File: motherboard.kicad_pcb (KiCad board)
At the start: 2 copper layers, 90.2 x 95.9 mm, 110 parts, among them P1 CONN_02X08, U1 STM32F411-LQFP64, U10 74LS125, U11 74LS125, U12 74LS125, U13 74LS125, U14 PCA9517A, U15 PCA9517A, U16 74LS125, U17 74LS125, U2 STM32F411-LQFP64, U3 AP7313, U4 74LS00, U5 74LS125, U6 FM25V20A-G, U7 FM25V20A-G, U8 FM25V20A-G, U9 FM25V20A-G, Y1 32k, Y2 8M(16pF), Y3 32k, Y4 8M(16pF)

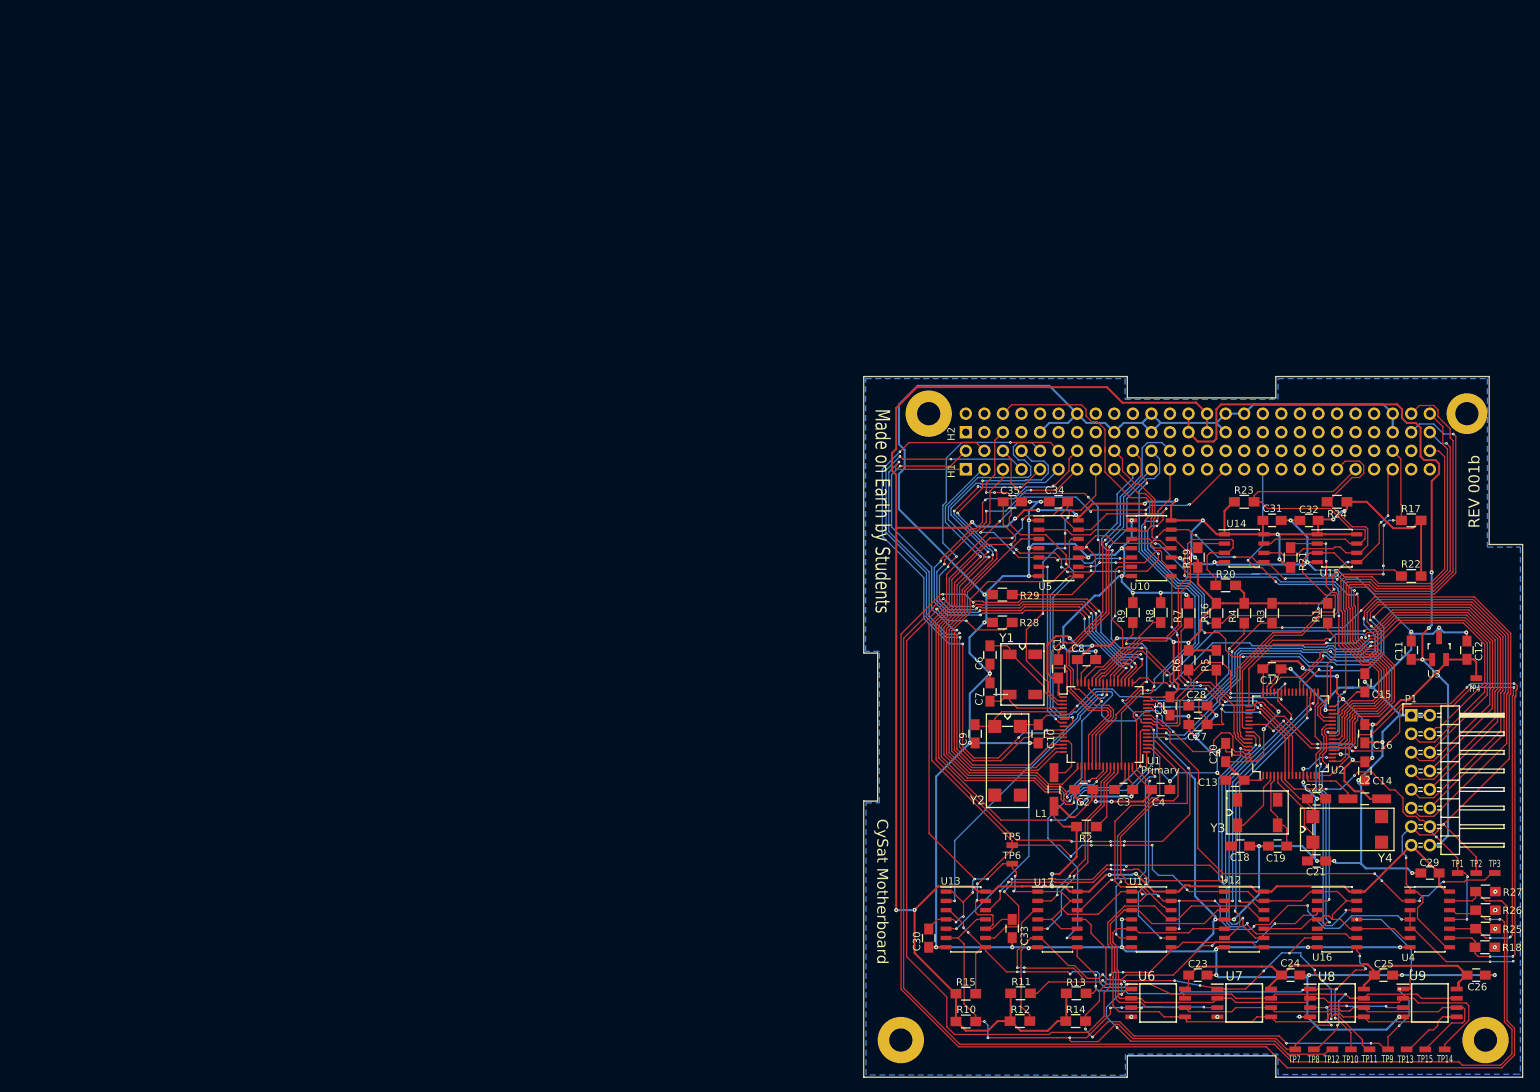
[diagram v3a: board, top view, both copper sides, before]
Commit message: Partial rerouting following resistor movement
Moving the fixed Pull-Up resistors to NAND output made a bunch of
traces have to move.

Not yet complete.
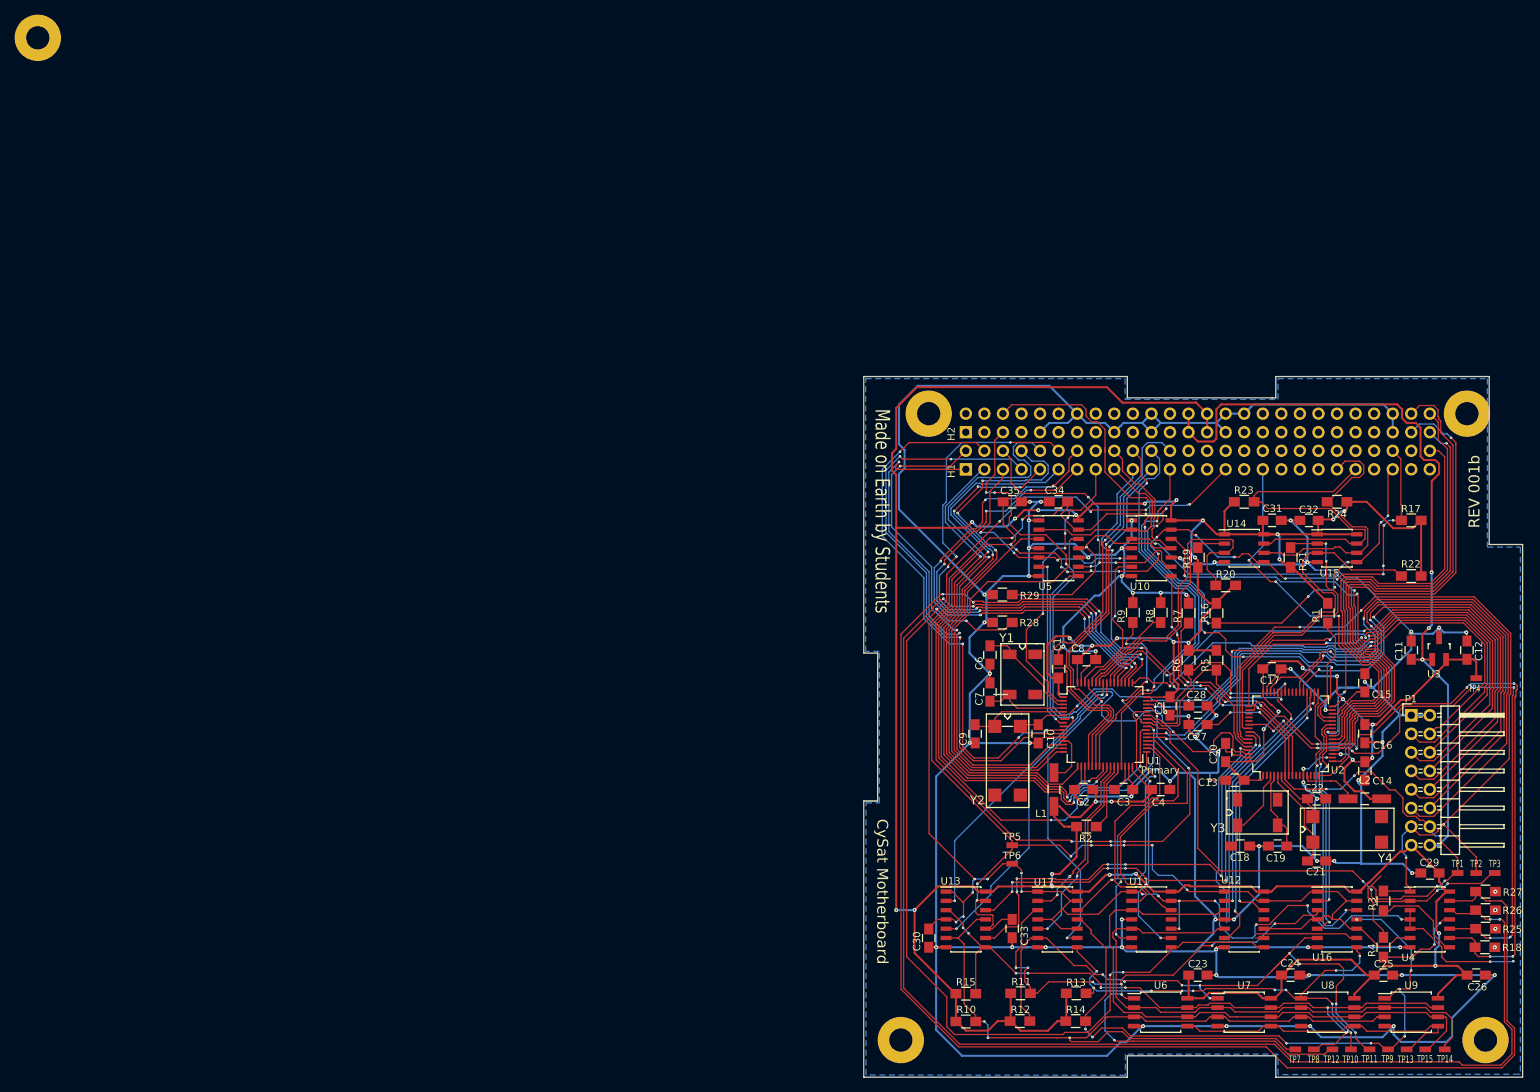
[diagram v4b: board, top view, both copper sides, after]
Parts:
- added REF**: Hole_0.125-0.250, Hole_0.125-0.250, F.Cu at (0.00, 0.00)
- U6, U7, U8, U9: footprint FM25V20A-G:SOIC127P800X203-8N -> Housings_SOIC:SOIJ-8_5.3x5.3mm_Pitch1.27mm
- moved R4 49.5 mm to (184.2, 124.5)
- moved R3 42.2 mm to (184.2, 118.1)
- moved U9 2.84 mm to (188.0, 133.3)
- moved U8 1.80 mm to (176.5, 133.3)
- moved U6 1.32 mm to (153.7, 133.3)
- moved U7 1.27 mm to (165.1, 133.3)
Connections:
- net /NRST1_P renamed /RST1_P
- net /NRST1_S renamed /RST1_S
- net /NRST2_P renamed /RST2_P
- net /NRST2_S renamed /RST2_S
- C33 pad 1: Net-(C33-Pad1) -> /NBUFEN_SEC
- C33 pad 2: Net-(C33-Pad2) -> GND
- C35 pad 1: Net-(C35-Pad1) -> /NBUFEN_SEC
- C35 pad 2: Net-(C35-Pad2) -> GND
- R3 pad 1: /NRST_P -> Net-(R3-Pad1)
- R3 pad 2: +3V3 -> /NRST_P
- R4 pad 1: /NRST_S -> Net-(R4-Pad1)
- R4 pad 2: +3V3 -> /NRST_S
- U4 pad 11: /NRST_S -> Net-(R4-Pad1)
- U4 pad 8: /NRST_P -> Net-(R3-Pad1)
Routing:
- net GND: track 725.5 -> 818.6 mm
- net /MEM_MOSI: track 94.4 -> 42.2 mm
- net Net-(R4-Pad1): track 0.00 -> 12.9 mm, vias 0 -> 2
- net Net-(R3-Pad1): track 0.00 -> 12.7 mm
- net +3V3: track 549.7 -> 558.8 mm, vias 25 -> 27
- net /NRST_P: track 140.2 -> 132.1 mm
- net /NBUFEN_SEC: track 235.4 -> 243.4 mm
- net /MEM_CS2: track 78.2 -> 85.8 mm
- net Net-(C35-Pad1): track 5.90 -> 0.00 mm
- net /SYS_RESET_S: track 42.7 -> 36.9 mm, vias 2 -> 1
- net /MEM_CS1_S: track 46.1 -> 41.1 mm, vias 2 -> 1
- net /MEM_SCK: track 87.1 -> 82.2 mm
- net /NRST_S: track 81.5 -> 77.2 mm, vias 9 -> 7
- net /MEM_MISO: track 82.3 -> 78.2 mm
- net /MEM_NHOLD: track 94.4 -> 92.0 mm
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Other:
- net class Power: clearance 0.2794 -> 0.1778

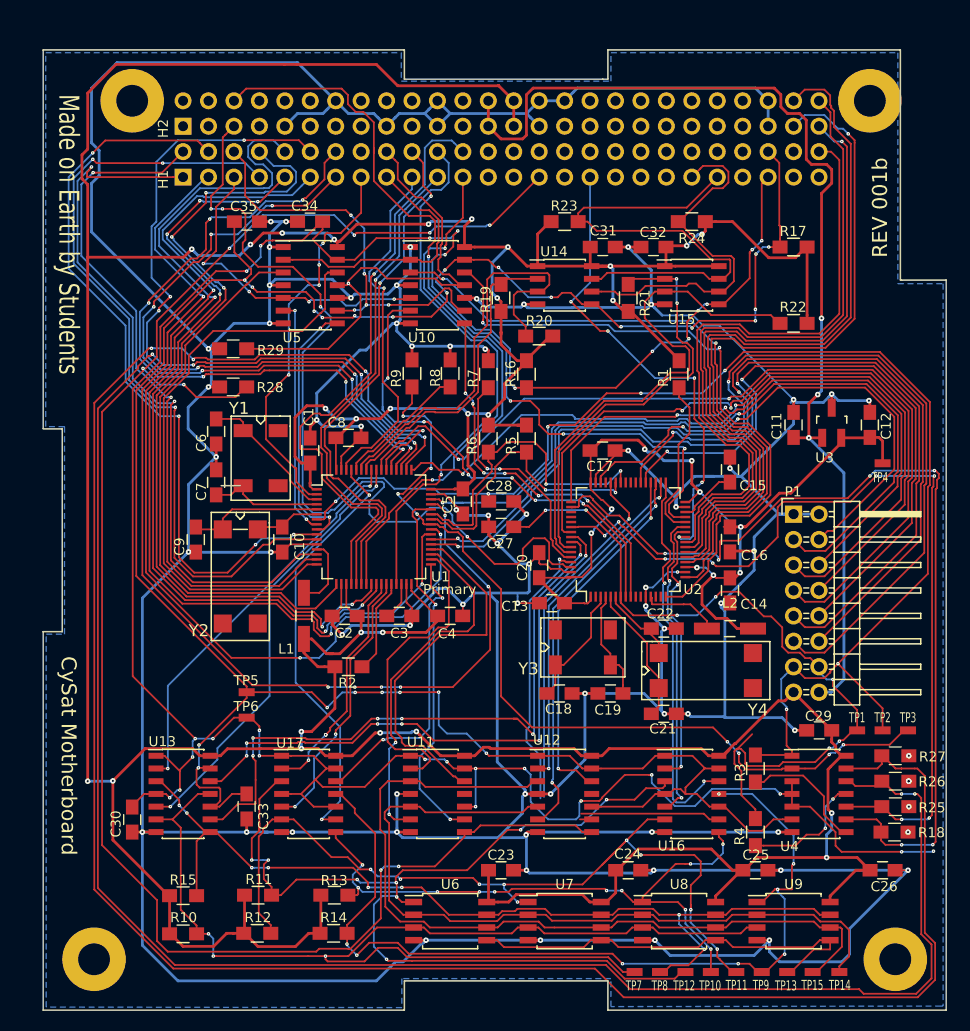
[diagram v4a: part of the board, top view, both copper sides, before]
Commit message: Finished Rev2 reworks
- Addressed documented issues
- Some SGPIO is not connected (see schematic for details)
- Created direct return paths for MEM_SPI
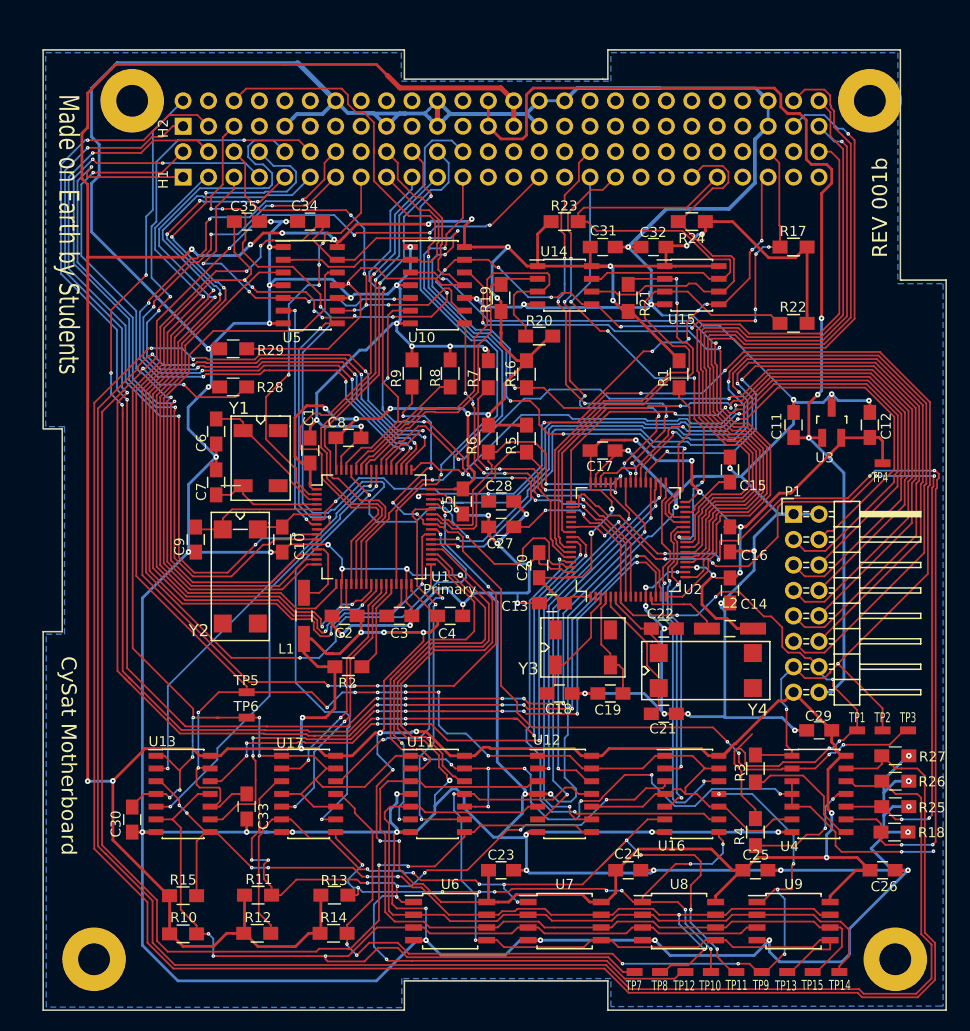
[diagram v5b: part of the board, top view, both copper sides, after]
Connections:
- H1 pad 36: /SGPIO10 -> Net-(H1-Pad36)
- H1 pad 37: /SGPIO11 -> Net-(H1-Pad37)
- H1 pad 38: /SGPIO12 -> Net-(H1-Pad38)
- H1 pad 39: /SGPIO13 -> Net-(H1-Pad39)
- H1 pad 50: /SGPIO5 -> Net-(H1-Pad50)
- H2 pad 4: /SGPIO3 -> Net-(H2-Pad4)
- H2 pad 7: /SGPIO4 -> Net-(H2-Pad7)
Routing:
- net GND: track 818.6 -> 997.0 mm, vias 71 -> 78
- net /SGPIO2: track 0.00 -> 143.8 mm, vias 0 -> 8
- net /SGPIO0: track 0.00 -> 139.7 mm, vias 0 -> 8
- net /SGPIO1: track 0.00 -> 133.0 mm, vias 0 -> 9
- net /SGPIO8: track 0.00 -> 45.7 mm, vias 0 -> 6
- net /SGPIO9: track 0.00 -> 43.6 mm, vias 0 -> 6
- net +3V3: track 558.8 -> 599.6 mm, vias 27 -> 31
- net /MEM_MOSI: track 42.2 -> 73.5 mm, vias 0 -> 2
- net /SYS_RESET_S: track 36.9 -> 41.9 mm, vias 1 -> 2
- net /MEM_CS1_S: track 41.1 -> 45.9 mm, vias 1 -> 2
- net /GPIO8: track 98.8 -> 102.3 mm
- net /NBUFEN_PRI: track 272.6 -> 275.9 mm, vias 29 -> 28
- net /MEM_SCK_P: track 30.9 -> 32.9 mm
- net /MEM_CS1_P: track 42.7 -> 44.7 mm
- net /SYS_RESET_P: track 36.9 -> 38.6 mm
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
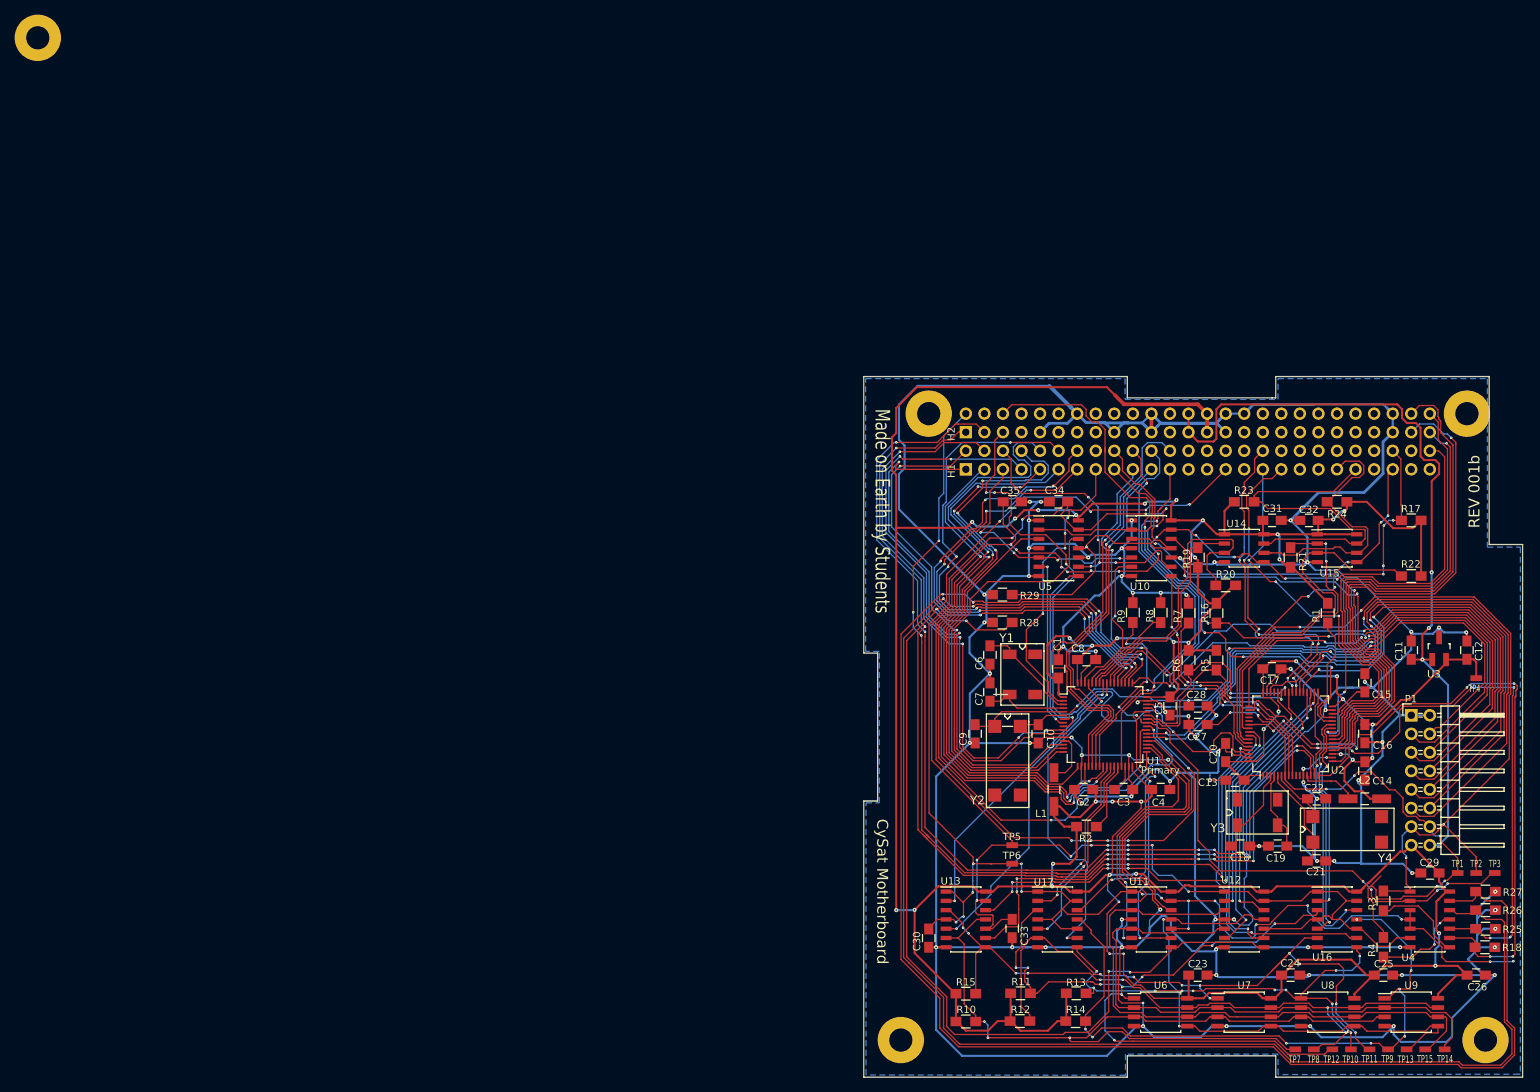
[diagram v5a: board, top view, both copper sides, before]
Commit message: Changed revision number on board
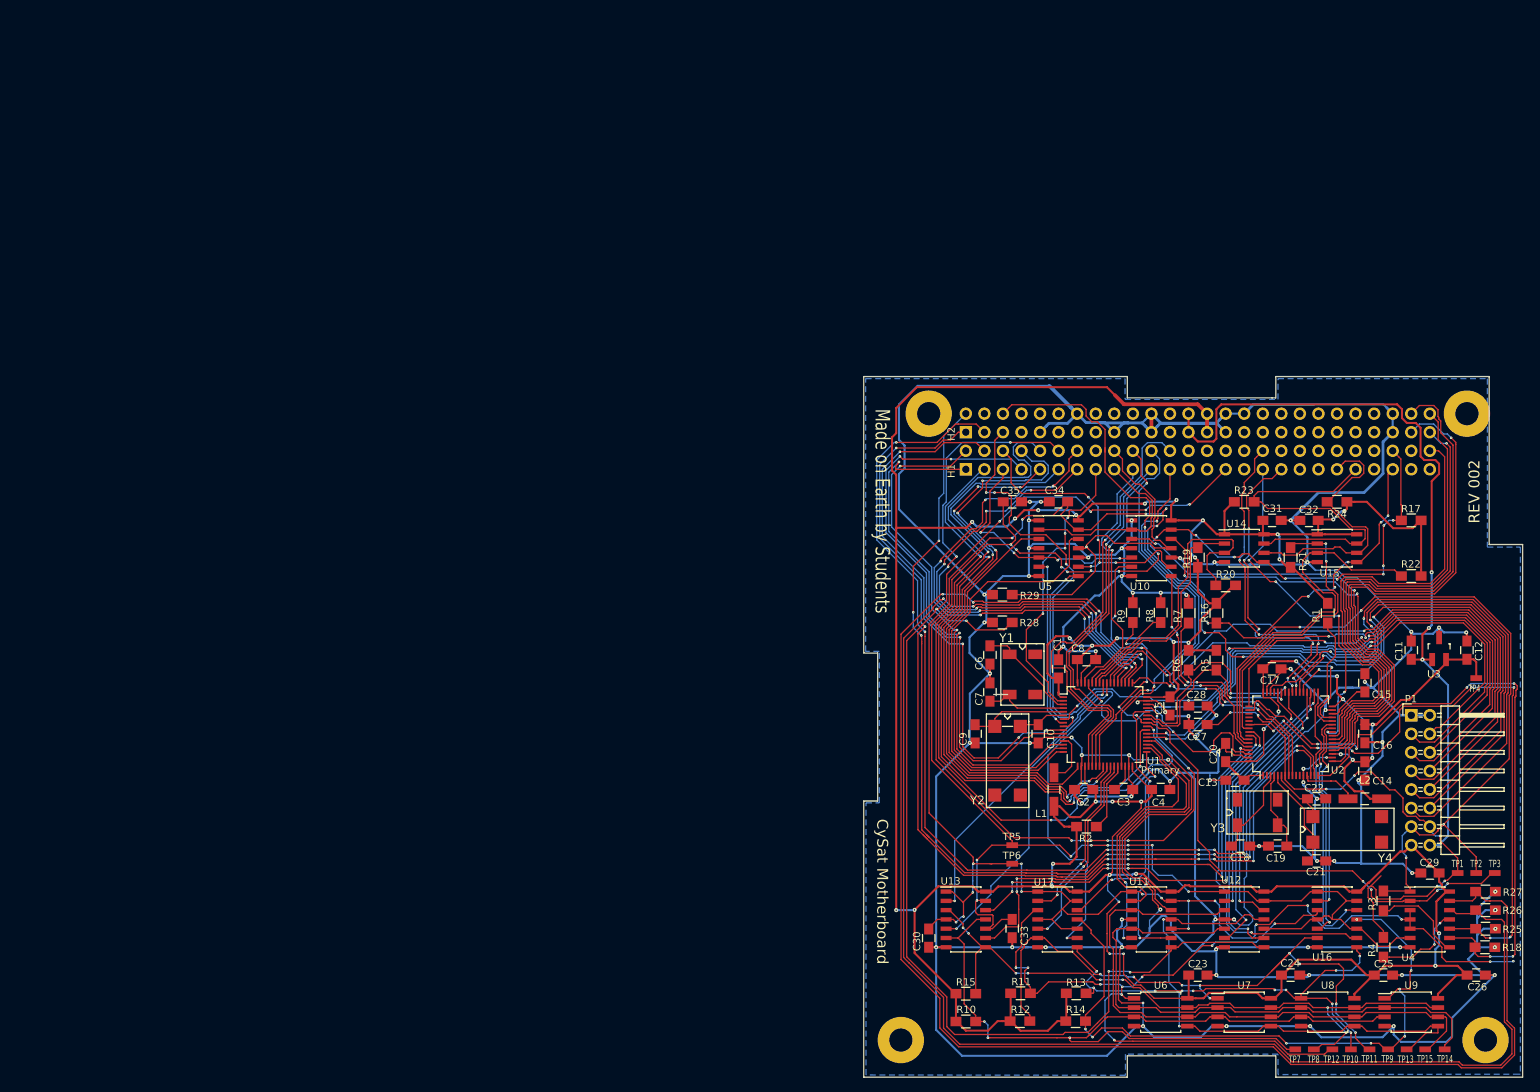
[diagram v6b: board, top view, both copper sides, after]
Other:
- board text added: "REV 002"
- board text removed: "REV 001b"
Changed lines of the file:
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@@
-(kicad_pcb (version 4) (host pcbnew 4.0.4-stable)
+(kicad_pcb (version 4) (host pcbnew 4.0.7)
   (general
     (links 387)
     (no_connects 0)
-    (area 112.954999 46.279999 203.275001 142.315001)
+    (area -7.130181 -3.4928 205.250181 142.315001)
     (thickness 1.6)
     (drawings 25)
@@
       (effects (font (size 1 1) (thickness 0.15)))
     )
-    (pad "" np_thru_hole circle (at 0 0) (size 6.35 6.35) (drill 3.175) (layers *.Cu *.Mask))
   )
   (module Housings_SOIC:SOIJ-8_5.3x5.3mm_Pitch1.27mm (layer F.Cu)
@@
   )
   (gr_line (start 113.03 84.201) (end 114.935 84.201) (layer Edge.Cuts) (width 0.15))
-  (gr_text "REV 001b" (at 196.596 62.103 90) (layer F.SilkS)
+  (gr_text "REV 002" (at 196.596 62.103 90) (layer F.SilkS)
     (effects (font (size 1.5 1.5) (thickness 0.3)))
   )
@@
     (connect_pads (clearance 0.508))
     (min_thickness 0.254)
-    (fill yes (arc_segments 16) (thermal_gap 0.508) (thermal_bridge_width 0.508))
+    (fill (arc_segments 16) (thermal_gap 0.508) (thermal_bridge_width 0.508))
     (polygon
       (pts
